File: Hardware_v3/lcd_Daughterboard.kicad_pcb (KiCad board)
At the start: 2 copper layers, 68 x 45 mm, 5 parts, among them J3 Conn_01x03_Pin, J4 Conn_01x03_Pin, J5 Conn_01x02_Pin, J6 Conn_01x02_Pin, U1 ILI9341_SPI_Bare

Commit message: Started working on panel
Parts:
- added U2: ILI9341_SPI_Daughterboard, Custom_Footprints:ILI9341_SPI_daughterboard_v2, F.Cu at (183.8, 56.4)
- moved J6 2.56 mm to (102.1, 136.5)
- moved J5 2.54 mm to (102.1, 106.0)
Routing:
- net +3.3V: track 41.1 -> 42.2 mm
- net /BackLight: track 24.2 -> 25.3 mm
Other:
- board text added: "BL"
- board text removed: "ANODE"
- board text removed: "BackLight"
- board text removed: "MISO"

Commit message: Control Layout change
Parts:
- moved U2 22.9 mm to (206.7, 56.6)
- moved J5 2.54 mm to (102.1, 108.5)
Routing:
- net /BackLight: track 25.3 -> 24.2 mm
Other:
- board text added: "LCD Daughterboard v3"
- board text removed: "LCD Daughterboard v2"
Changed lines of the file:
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@@
 	(footprint "Custom_Footprints:ILI9341_SPI_daughterboard_v2"
 		(layer "F.Cu")
-		(at 183.8 56.4)
+		(at 206.7 56.6)
 		(descr "ILI9341 LCD")
 		(tags "ILI9341 LCD SPI")
@@
 		(attr through_hole board_only exclude_from_pos_files exclude_from_bom dnp)
 		(fp_rect
-			(start -1 -3.54)
-			(end 1 1.06)
+			(start -1 -1)
+			(end 1 3.6)
 			(stroke
 				(width 0.12)
@@
 			)
 		)
+		(fp_text user "SCK"
+			(at 62.502381 22.86 0)
+			(unlocked yes)
+			(layer "F.SilkS")
+			(effects
+				(font
+					(size 1 1)
+					(thickness 0.15)
+				)
+				(justify right)
+			)
+		)
+		(fp_text user "3.3V"
+			(at 3.144047 30.5 0)
+			(unlocked yes)
+			(layer "F.SilkS")
+			(effects
+				(font
+					(size 1 1)
+					(thickness 0.15)
+				)
+			)
+		)
 		(fp_text user "BL"
 			(at 1.4 -0.04 0)
@@
 			)
 		)
+		(fp_text user "DC"
+			(at 60.2 0 0)
+			(unlocked yes)
+			(layer "F.SilkS")
+			(effects
+				(font
+					(size 1 1)
+					(thickness 0.15)
+				)
+				(justify left)
+			)
+		)
 		(fp_text user "GND"
 			(at 62.502381 25.46 0)
@@
 		)
 		(fp_text user "GND"
-			(at 3.048809 27.9 0)
-			(unlocked yes)
-			(layer "F.SilkS")
-			(effects
-				(font
-					(size 1 1)
-					(thickness 0.15)
-				)
-			)
-		)
-		(fp_text user "DC"
-			(at 60.2 0 0)
+			(at 59.152381 2.6 0)
 			(unlocked yes)
 			(layer "F.SilkS")
@@
 			)
 		)
-		(fp_text user "3.3V"
-			(at 3.144047 30.5 0)
+		(fp_text user "GND"
+			(at 1.4 0.1 0)
 			(unlocked yes)
 			(layer "F.SilkS")
@@
 					(thickness 0.15)
 				)
+				(justify left)
 			)
 		)
 		(fp_text user "GND"
-			(at 1.4 -2.44 0)
+			(at 3.048809 27.9 0)
 			(unlocked yes)
 			(layer "F.SilkS")
@@
 					(thickness 0.15)
 				)
-				(justify left)
-			)
-		)
-		(fp_text user "GND"
-			(at 59.152381 2.6 0)
-			(unlocked yes)
-			(layer "F.SilkS")
-			(effects
-				(font
-					(size 1 1)
-					(thickness 0.15)
-				)
-				(justify left)
-			)
-		)
-		(fp_text user "SCK"
-			(at 62.502381 22.86 0)
-			(unlocked yes)
-			(layer "F.SilkS")
-			(effects
-				(font
-					(size 1 1)
-					(thickness 0.15)
-				)
-				(justify right)
 			)
 		)
@@
 			(layer "Cmts.User")
 			(pts
-				(xy 184.95 92.3) (xy 193.95 92.3)
-			)
-			(height -53.9)
-			(gr_text "9.0000 mm"
-				(at 189.7 36.7 0)
+				(xy 216.4 89.05) (xy 216.4 52.05)
+			)
+			(height 65.6)
+			(gr_text "37.0000 mm"
+				(at 283.55 70.65 90)
 				(layer "Cmts.User")
 				(effects
@@
 			(layer "Cmts.User")
 			(pts
-				(xy 184.5 88.85) (xy 184.5 91.85)
+				(xy 207.4 49.05) (xy 207.4 52.05)
 			)
 			(height -74.6)
 			(gr_text "3.0000 mm"
-				(at 261.3 89.9 90)
+				(at 283.8 50.9 90)
 				(layer "Cmts.User")
 				(effects
@@
 			(layer "Cmts.User")
 			(pts
-				(xy 184.5 48.85) (xy 184.5 51.85)
-			)
-			(height -74.6)
-			(gr_text "3.0000 mm"
-				(at 260.9 50.7 90)
+				(xy 216.85 88.6) (xy 265.85 88.6)
+			)
+			(height -50)
+			(gr_text "49.0000 mm"
+				(at 241.35 37.15 0)
 				(layer "Cmts.User")
 				(effects
@@
 			(layer "Cmts.User")
 			(pts
-				(xy 242.95 92.3) (xy 245.45 92.3)
-			)
-			(height -53.9)
-			(gr_text "2.5000 mm"
-				(at 244.5 36.5 0)
+				(xy 207.4 89.05) (xy 207.4 92.05)
+			)
+			(height -74.6)
+			(gr_text "3.0000 mm"
+				(at 284.2 90.1 90)
 				(layer "Cmts.User")
 				(effects
@@
 			(layer "Cmts.User")
 			(pts
-				(xy 193.95 88.4) (xy 242.95 88.4)
-			)
-			(height -50)
-			(gr_text "49.0000 mm"
-				(at 218.45 36.95 0)
+				(xy 265.85 92.5) (xy 268.35 92.5)
+			)
+			(height -53.9)
+			(gr_text "2.5000 mm"
+				(at 267.4 36.7 0)
 				(layer "Cmts.User")
 				(effects
@@
 			(layer "Cmts.User")
 			(pts
-				(xy 193.5 88.85) (xy 193.5 51.85)
-			)
-			(height 65.6)
-			(gr_text "37.0000 mm"
-				(at 260.65 70.45 90)
+				(xy 207.85 92.5) (xy 216.85 92.5)
+			)
+			(height -53.9)
+			(gr_text "9.0000 mm"
+				(at 212.6 36.9 0)
 				(layer "Cmts.User")
 				(effects
@@
 		)
 		(pad "7" thru_hole rect
-			(at 0 -2.54)
+			(at 0 0)
 			(size 1.5 1.5)
 			(drill 1)
@@
 		)
 		(pad "8" thru_hole circle
-			(at 0 0)
+			(at 0 2.54)
 			(size 1.5 1.5)
 			(drill 1)
@@
 	(footprint "Connector_PinHeader_2.54mm:PinHeader_1x02_P2.54mm_Vertical"
 		(layer "B.Cu")
-		(at 102.1 105.96 180)
+		(at 102.1 108.5 180)
 		(descr "Through hole straight pin header, 1x02, 2.54mm pitch, single row")
 		(tags "Through hole pin header THT 1x02 2.54mm single row")
@@
 	(footprint "Connector_PinHeader_2.54mm:PinHeader_1x02_P2.54mm_Vertical"
 		(layer "B.Cu")
-		(at 102.1 136.46 180)
+		(at 102.1 136.5 180)
 		(descr "Through hole straight pin header, 1x02, 2.54mm pitch, single row")
 		(tags "Through hole pin header THT 1x02 2.54mm single row")
@@
 		(layer "Edge.Cuts")
 	)
-	(gr_text "LCD Daughterboard v2"
+	(gr_text "LCD Daughterboard v3"
 		(at 135.4 102.1 0)
 		(layer "B.SilkS")
@@
 	)
 	(segment
-		(start 119 122.7)
-		(end 104.8 108.5)
-		(width 0.4)
-		(layer "F.Cu")
-		(net 10)
-	)
-	(segment
-		(start 104.8 108.5)
-		(end 102.1 108.5)
-		(width 0.4)
-		(layer "F.Cu")
-		(net 10)
-	)
-	(segment
 		(start 121.5 122.7)
 		(end 119 122.7)
 		(width 0.4)
 		(layer "F.Cu")
+		(net 10)
+	)
+	(segment
+		(start 119 122.7)
+		(end 107.34 111.04)
+		(width 0.4)
+		(layer "F.Cu")
+		(net 10)
+	)
+	(segment
+		(start 107.34 111.04)
+		(end 102.1 111.04)
+		(width 0.4)
+		(layer "F.Cu")

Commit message: More layout
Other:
- board text added: "3v3"
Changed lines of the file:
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@@
+	)
+	(gr_line
+		(start 121.7 129.7)
+		(end 121.7 131.4)
+		(stroke
+			(width 0.15)
+			(type default)
+		)
+		(layer "F.SilkS")
 	)
 	(gr_line
@@
 	)
 	(gr_line
+		(start 121.7 113.2)
+		(end 121.7 114.9)
+		(stroke
+			(width 0.15)
+			(type default)
+		)
+		(layer "F.SilkS")
+	)
+	(gr_line
 		(start 123.1 119.5)
 		(end 125.45 120.4)
-		(stroke
-			(width 0.15)
-			(type default)
-		)
-		(layer "F.SilkS")
-	)
-	(gr_line
-		(start 123.1 116.3)
-		(end 125.4 114.85)
-		(stroke
-			(width 0.15)
-			(type default)
-		)
-		(layer "F.SilkS")
-	)
-	(gr_line
-		(start 123.1 117.9)
-		(end 125.45 117.65)
-		(stroke
-			(width 0.15)
-			(type default)
-		)
-		(layer "F.SilkS")
-	)
-	(gr_line
-		(start 123.1 117.05)
-		(end 125.45 116.25)
 		(stroke
 			(width 0.15)
@@
 		(end 161.25 140.95)
 		(stroke
+			(width 0.3)
+			(type default)
+		)
+		(fill none)
+		(layer "F.SilkS")
+	)
+	(gr_line
+		(start 123.1 116.3)
+		(end 125.4 114.85)
+		(stroke
+			(width 0.15)
+			(type default)
+		)
+		(layer "F.SilkS")
+	)
+	(gr_line
+		(start 123.1 117.9)
+		(end 125.45 117.65)
+		(stroke
+			(width 0.15)
+			(type default)
+		)
+		(layer "F.SilkS")
+	)
+	(gr_line
+		(start 123.1 117.05)
+		(end 125.45 116.25)
+		(stroke
+			(width 0.15)
+			(type default)
+		)
+		(layer "F.SilkS")
+	)
+	(gr_rect
+		(start 112.25 103.95)
+		(end 161.25 140.95)
+		(stroke
 			(width 0.2)
 			(type default)
@@
 		(layer "F.SilkS")
 		(effects
+			(font
+				(size 1 1)
+				(thickness 0.15)
+			)
+		)
+	)
+	(gr_text "3v3"
+		(at 101.8 141.9 0)
+		(layer "F.SilkS")
+		(effects
+			(font
+				(size 1 1)
+				(thickness 0.15)
+			)
+		)
+	)
+	(gr_text "BL"
+		(at 101.8 113.9 0)
+		(layer "F.SilkS")
+		(effects

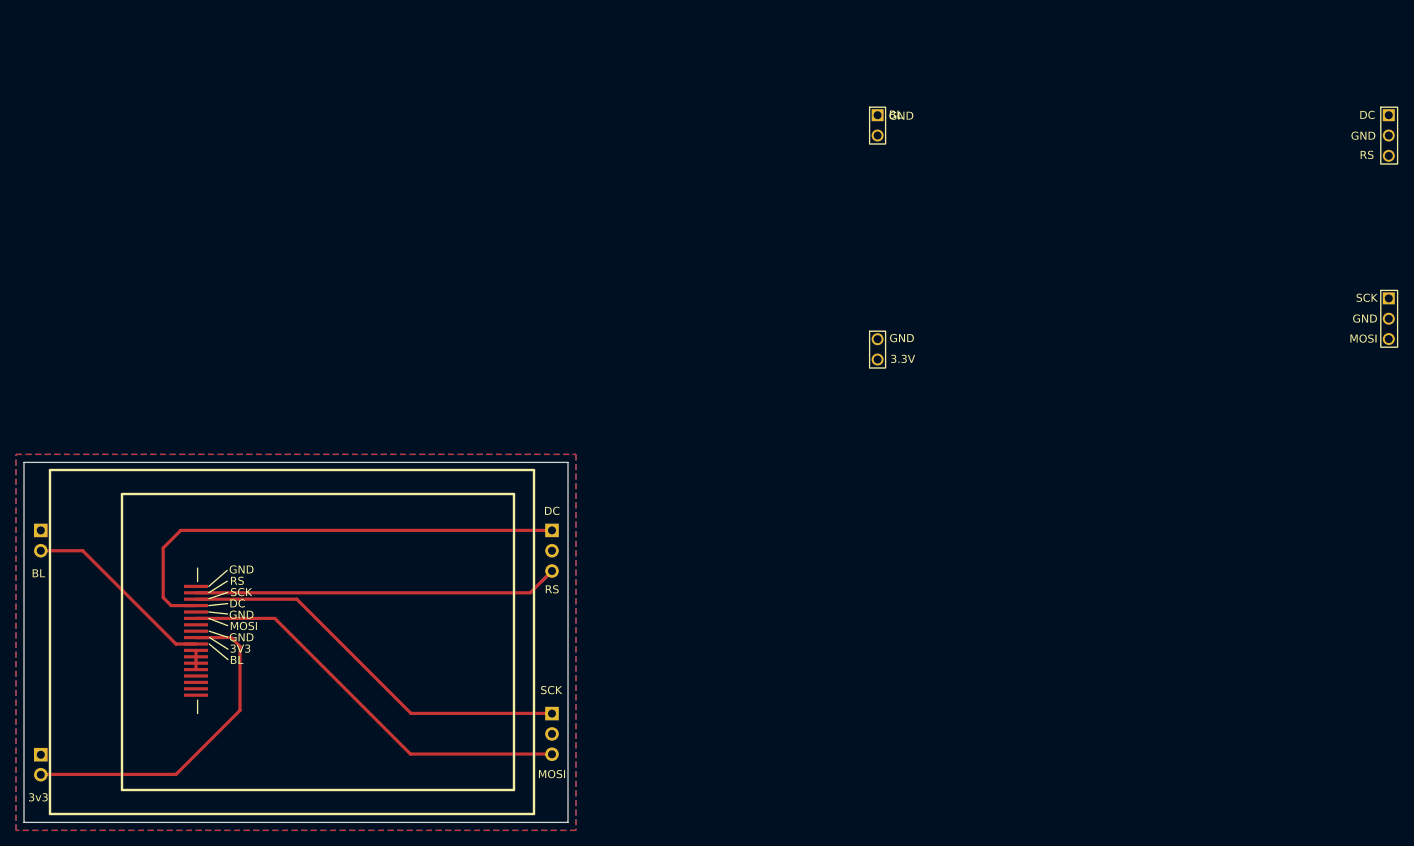
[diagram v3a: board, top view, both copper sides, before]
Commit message: V3 production files submitted to JLC
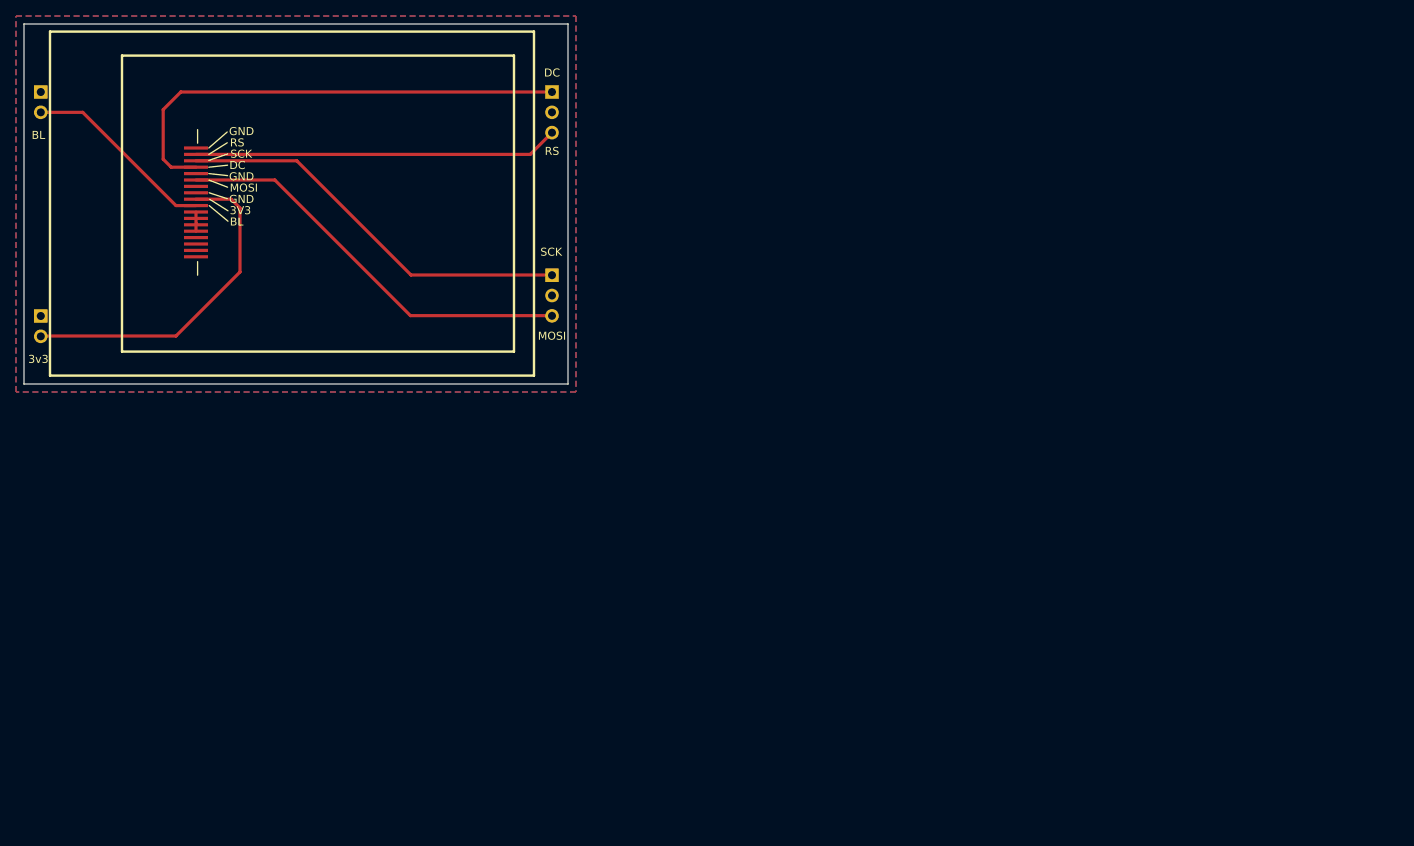
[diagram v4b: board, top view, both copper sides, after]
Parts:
- removed U2: ILI9341_SPI_Daughterboard, Custom_Footprints:ILI9341_SPI_daughterboard_v2
- moved J4 54.8 mm to (166.0, 76.6)
- moved J3 54.8 mm to (166.0, 53.7)
- moved J5 54.8 mm to (102.1, 53.7)
- moved J6 54.8 mm to (102.1, 81.7)
- moved U1 54.8 mm to (121.5, 60.7)
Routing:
- net /LCD_RESET: track 47.5 -> 45.6 mm
